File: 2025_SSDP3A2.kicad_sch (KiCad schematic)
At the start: 65 parts, among them J1 SolderPad, J2 SolderPad, J3 SolderPad, J4 SolderPad, Q1 CSD19534Q5A, Q2 BSC0805LS, U1 LM5146RGYR

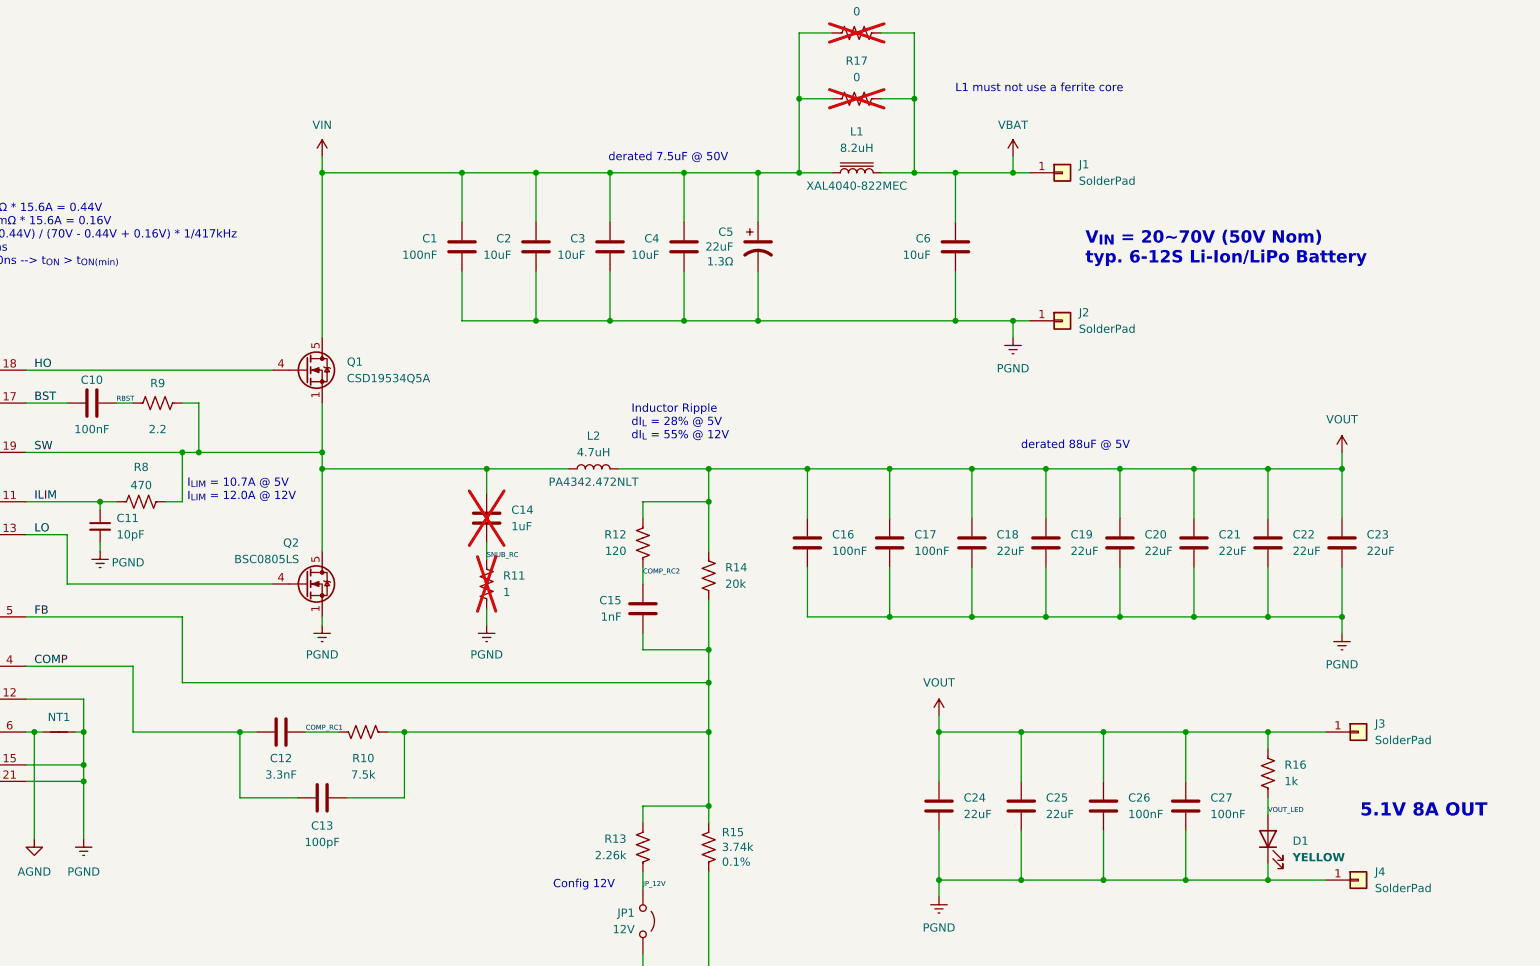
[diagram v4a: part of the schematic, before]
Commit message: Revised ILIM setting, added TVS
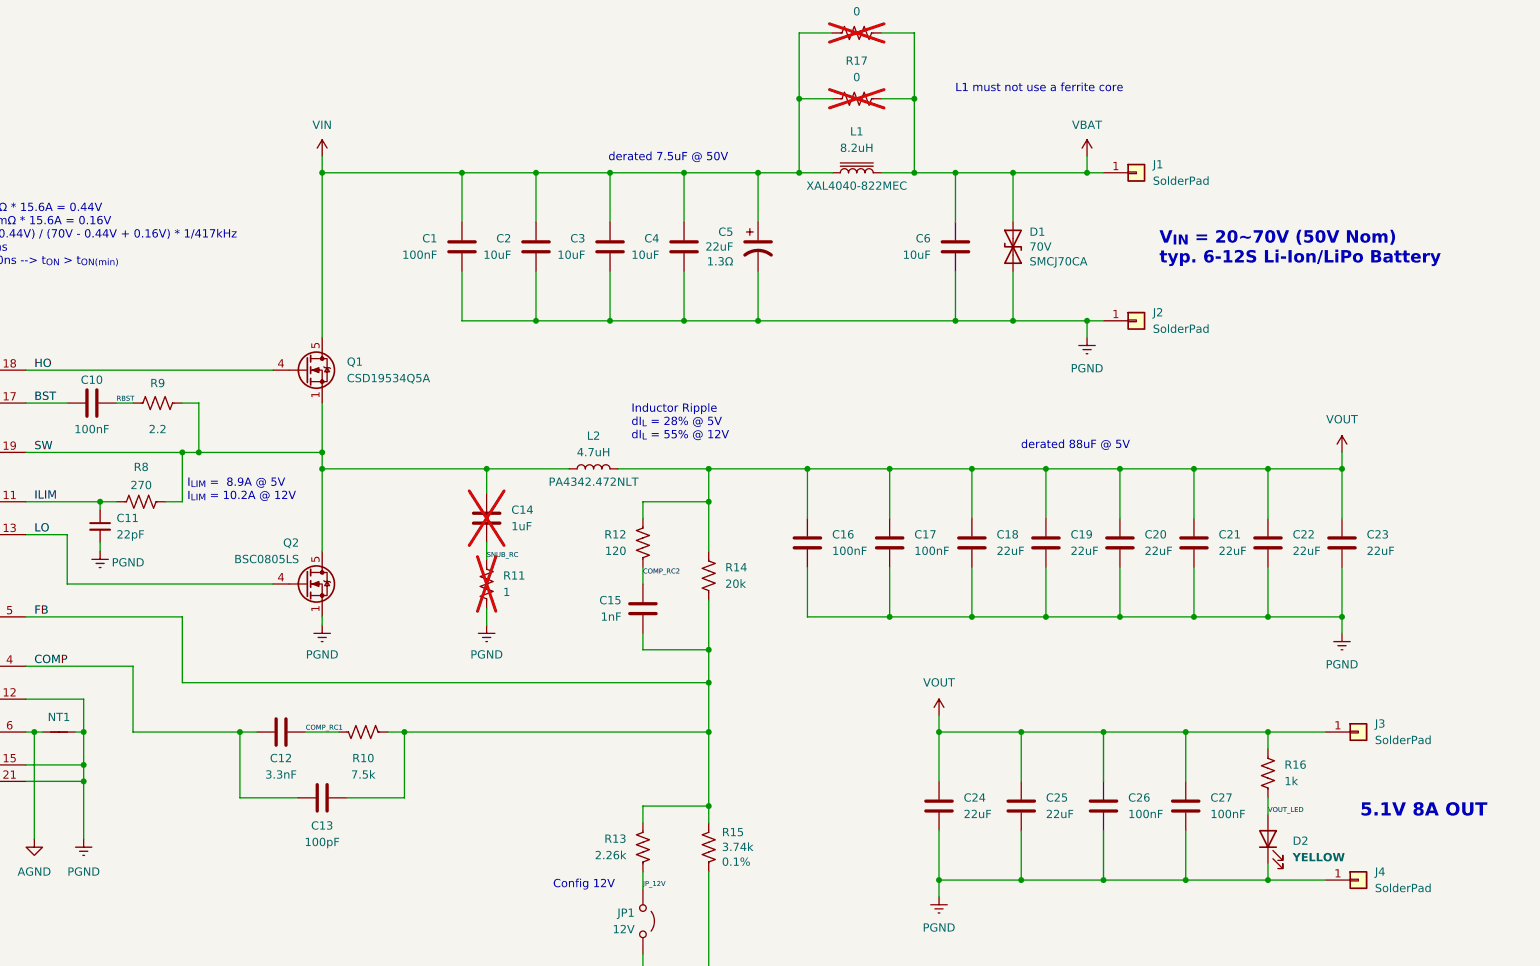
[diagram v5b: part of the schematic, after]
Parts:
- added D1: 70V, Diode_SMD:D_SMC, symbol Diode:1.5SMCxxCA
- C11: value 10pF -> 22pF; LCSC PN C126575 -> C408549
- R8: value 470 -> 270; LCSC PN C23179 -> C22966
- renumbered D1 to D2
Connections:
- net PGND: now also D1.2 (A2)
- net VBAT: now also D1.1 (A1)
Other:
- note added: "I_{LIM} = 8.9A @ 5V I_{LIM} = 10.2A @ 12V"
- note removed: "I_{LIM} = 10.7A @ 5V I_{LIM} = 12.0A @ 12V"
- moved on the sheet: J1, J2
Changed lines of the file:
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@@
 	(text "V_{IN} = 20~70V (50V Nom)\ntyp. 6-12S Li-Ion/LiPo Battery"
 		(exclude_from_sim no)
-		(at 321.056 96.774 0)
+		(at 332.486 96.774 0)
 		(effects
 			(font
@@
 		)
 	)
-	(text "I_{LIM} = 10.7A @ 5V\nI_{LIM} = 12.0A @ 12V"
+	(text "I_{LIM} =  8.9A @ 5V\nI_{LIM} = 10.2A @ 12V"
 		(exclude_from_sim no)
 		(at 182.372 134.112 0)
@@
 	)
 	(junction
-		(at 309.88 107.95)
+		(at 321.31 107.95)
 		(diameter 0)
 		(color 0 0 0 0)
@@
 	)
 	(junction
+		(at 309.88 107.95)
+		(diameter 0)
+		(color 0 0 0 0)
+	)
+	(junction
 		(at 337.82 130.81)
 		(diameter 0)
@@
 	)
 	(junction
+		(at 309.88 85.09)
+		(diameter 0)
+		(color 0 0 0 0)
+	)
+	(junction
 		(at 57.15 158.75)
 		(diameter 0)
@@
 	)
 	(junction
-		(at 309.88 85.09)
+		(at 321.31 85.09)
 		(diameter 0)
 		(color 0 0 0 0)
@@
 	(wire
 		(pts
+			(xy 309.88 107.95) (xy 321.31 107.95)
+		)
+		(stroke
+			(width 0)
+			(type default)
+		)
+	)
+	(wire
+		(pts
 			(xy 236.22 100.33) (xy 236.22 107.95)
 		)
@@
 	(wire
 		(pts
-			(xy 309.88 107.95) (xy 309.88 110.49)
+			(xy 321.31 107.95) (xy 321.31 110.49)
 		)
 		(stroke
@@
 	(wire
 		(pts
-			(xy 309.88 85.09) (xy 312.42 85.09)
+			(xy 321.31 85.09) (xy 323.85 85.09)
 		)
 		(stroke
@@
 	(wire
 		(pts
+			(xy 309.88 85.09) (xy 321.31 85.09)
+		)
+		(stroke
+			(width 0)
+			(type default)
+		)
+	)
+	(wire
+		(pts
 			(xy 262.89 163.83) (xy 262.89 171.45)
 		)
@@
 	(wire
 		(pts
-			(xy 309.88 107.95) (xy 312.42 107.95)
+			(xy 321.31 107.95) (xy 323.85 107.95)
 		)
 		(stroke
@@
 	(wire
 		(pts
+			(xy 309.88 85.09) (xy 309.88 92.71)
+		)
+		(stroke
+			(width 0)
+			(type default)
+		)
+	)
+	(wire
+		(pts
 			(xy 87.63 158.75) (xy 87.63 162.56)
 		)
@@
 	(wire
 		(pts
-			(xy 309.88 82.55) (xy 309.88 85.09)
+			(xy 321.31 82.55) (xy 321.31 85.09)
 		)
 		(stroke
@@
 	(wire
 		(pts
+			(xy 309.88 100.33) (xy 309.88 107.95)
+		)
+		(stroke
+			(width 0)
+			(type default)
+		)
+	)
+	(wire
+		(pts
 			(xy 278.13 130.81) (xy 278.13 138.43)
 		)
@@
 	(symbol
 		(lib_id "Connector_Generic:Conn_01x01")
-		(at 317.5 85.09 0)
+		(at 328.93 85.09 0)
 		(unit 1)
 		(exclude_from_sim no)
@@
 		(fields_autoplaced yes)
 		(property "Reference" "J1"
-			(at 320.04 83.82 0)
+			(at 331.47 83.82 0)
 			(effects
 				(font
@@
 		)
 		(property "Value" "SolderPad"
-			(at 320.04 86.36 0)
+			(at 331.47 86.36 0)
 			(effects
 				(font
@@
 		)
 		(property "Footprint" "Connector_Wire:SolderWirePad_1x01_SMD_3x6mm"
-			(at 317.5 85.09 0)
+			(at 328.93 85.09 0)
 			(effects
 				(font
@@
 		)
 		(property "Datasheet" "~"
-			(at 317.5 85.09 0)
+			(at 328.93 85.09 0)
 			(effects
 				(font
@@
 		)
 		(property "Description" "Generic connector, single row, 01x01, script generated (kicad-library-utils/schlib/autogen/connector/)"
-			(at 317.5 85.09 0)
+			(at 328.93 85.09 0)
 			(effects
 				(font
@@
 	(symbol
 		(lib_id "Connector_Generic:Conn_01x01")
-		(at 317.5 107.95 0)
+		(at 328.93 107.95 0)
 		(unit 1)
 		(exclude_from_sim no)
@@
 		(fields_autoplaced yes)
 		(property "Reference" "J2"
-			(at 320.04 106.68 0)
+			(at 331.47 106.68 0)
 			(effects
 				(font
@@
 		)
 		(property "Value" "SolderPad"
-			(at 320.04 109.22 0)
+			(at 331.47 109.22 0)
 			(effects
 				(font
@@
 		)
 		(property "Footprint" "Connector_Wire:SolderWirePad_1x01_SMD_3x6mm"
-			(at 317.5 107.95 0)
+			(at 328.93 107.95 0)
 			(effects
 				(font
@@
 		)
 		(property "Datasheet" "~"
-			(at 317.5 107.95 0)
+			(at 328.93 107.95 0)
 			(effects
 				(font
@@
 		)
 		(property "Description" "Generic connector, single row, 01x01, script generated (kicad-library-utils/schlib/autogen/connector/)"
-			(at 317.5 107.95 0)
+			(at 328.93 107.95 0)
 			(effects
 				(font
@@
 			)
 		)
-		(property "Value" "470"
+		(property "Value" "270"
 			(at 175.26 133.35 90)
 			(effects
@@
 			)
 		)
-		(property "Description" "0603WAF4700T5E"
+		(property "Description" "0603WAF2700T5E"
 			(at 175.26 135.89 0)
 			(effects
@@
 			)
 		)
-		(property "LCSC PN" "C23179"
+		(property "LCSC PN" "C22966"
 			(at 175.26 135.89 90)
 			(effects
@@
 	(symbol
 		(lib_id "power:VDD")
-		(at 309.88 82.55 0)
+		(at 321.31 82.55 0)
 		(mirror y)
 		(unit 1)
@@
 		(dnp no)
 		(property "Reference" "#PWR021"
-			(at 309.88 86.36 0)
+			(at 321.31 86.36 0)
 			(effects
 				(font
@@
 		)
 		(property "Value" "VBAT"
-			(at 309.88 77.724 0)
+			(at 321.31 77.724 0)
 			(effects
 				(font
@@
 		)
 		(property "Footprint" ""
-			(at 309.88 82.55 0)
+			(at 321.31 82.55 0)
 			(effects
 				(font
@@
 		)
 		(property "Datasheet" ""
-			(at 309.88 82.55 0)
+			(at 321.31 82.55 0)
 			(effects
 				(font
@@
 		)
 		(property "Description" "Power symbol creates a global label with name \"VDD\""
-			(at 309.88 82.55 0)
+			(at 321.31 82.55 0)
 			(effects
 				(font
@@
 			)
 		)
-		(property "Value" "10pF"
+		(property "Value" "22pF"
 			(at 171.45 140.9763 0)
 			(effects
@@
 			)
 		)
-		(property "Description" "GCM1885C2A100JA16D"
+		(property "Description" "GCM1885C2A220JA16D"
 			(at 168.91 139.7 0)
 			(effects
@@
 			)
 		)
-		(property "LCSC PN" "C126575"
+		(property "LCSC PN" "C408549"
 			(at 168.91 139.7 0)
 			(effects
@@
 		(dnp no)
 		(fields_autoplaced yes)
-		(property "Reference" "D1"
+		(property "Reference" "D2"
 			(at 353.06 188.2775 90)
 			(effects
@@
 			(project "2025_SSDP3A1"
 				(path "/ea689c3b-fea3-4fc0-9d65-1fb672b240d8"
-					(reference "D1")
+					(reference "D2")
 					(unit 1)
 				)
@@
 	(symbol
 		(lib_id "power:Earth")
-		(at 309.88 110.49 0)
+		(at 321.31 110.49 0)
 		(mirror y)
 		(unit 1)
@@
 		(dnp no)
 		(property "Reference" "#PWR022"
-			(at 309.88 116.84 0)
+			(at 321.31 116.84 0)
 			(effects
 				(font
@@
 		)
 		(property "Value" "PGND"
-			(at 309.88 115.316 0)
+			(at 321.31 115.316 0)
 			(effects
 				(font
@@
 		)
 		(property "Footprint" ""
-			(at 309.88 110.49 0)
+			(at 321.31 110.49 0)
 			(effects
 				(font
@@
 		)
 		(property "Datasheet" "~"
-			(at 309.88 110.49 0)
+			(at 321.31 110.49 0)
 			(effects
 				(font
@@
 		)
 		(property "Description" "Power symbol creates a global label with name \"Earth\""
-			(at 309.88 110.49 0)
+			(at 321.31 110.49 0)
 			(effects
 				(font
@@
 					(unit 1)
 				)
+			)
+		)
+	)
+	(symbol
+		(lib_id "Diode:1.5SMCxxCA")
+		(at 309.88 96.52 270)
+		(unit 1)
+		(exclude_from_sim no)
+		(in_bom yes)
+		(on_board yes)
+		(dnp no)
+		(property "Reference" "D1"
+			(at 312.42 94.234 90)
+			(effects
+				(font
+					(size 1.27 1.27)
+				)
+				(justify left)
+			)
+		)
+		(property "Value" "70V"
+			(at 312.42 96.52 90)
+			(effects
+				(font
+					(size 1.27 1.27)
+				)
+				(justify left)
+			)
+		)
+		(property "Footprint" "Diode_SMD:D_SMC"
+			(at 304.8 96.52 0)
+			(effects
+				(font
+					(size 1.27 1.27)
+				)
+				(hide yes)
+			)
+		)
+		(property "Datasheet" "https://www.vishay.com/docs/88303/15smc.pdf"
+			(at 309.88 96.52 0)
+			(effects
+				(font
+					(size 1.27 1.27)
+				)
+				(hide yes)
+			)
+		)
+		(property "Description" "SMCJ70CA"
+			(at 312.42 98.806 90)
+			(effects
+				(font
+					(size 1.27 1.27)
+				)
+				(justify left)
+			)
+		)
+		(pin "2"
+		)
+		(pin "1"
+		)
+		(instances
+			(project ""
+				(path "/ea689c3b-fea3-4fc0-9d65-1fb672b240d8"
+					(reference "D1")
+					(unit 1)
+				)
